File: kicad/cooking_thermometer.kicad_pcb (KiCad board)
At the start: 2 copper layers, 75.5 x 40.4 mm, 60 parts, among them J1 FTDI, J2 STLINK, J3 3V3_Power, J4 Battery, J6 OLED_CONN, J7 5V_Power, J8 THERMO_CONN, J9 USB_C, Q1 BC547, SW1 BOOT0_SW, SW2 NRST_SW, SW3 UI_A_SW, SW4 UI_B_SW, SW5 UI_C_SW, U1 STM32G0B0KETx, U2 MCP1700x-330xxTO, U3 MCP73831-2-OT

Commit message: Final silk fixes
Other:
- board text added: "5V"
- board text added: "A"
- board text added: "B"
- board text added: "BOOT0"
- board text added: "C"
- board text added: "RST"
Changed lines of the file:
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@@
 		(tags "tact sw push 6mm")
 		(property "Reference" "SW4"
-			(at 3.25 -2 0)
+			(at 6.388 -1.95 0)
 			(layer "F.SilkS")
 			(effects
@@
 		(tags "tact sw push 6mm")
 		(property "Reference" "SW5"
-			(at 3.25 -2 0)
+			(at 6.348 -2 0)
 			(layer "F.SilkS")
 			(effects
@@
 		(tags "mounting hole 3.2mm no annular m3")
 		(property "Reference" "H5"
-			(at 0 -4.2 0)
+			(at 4.6 1.1 0)
 			(layer "F.SilkS")
 			(effects
@@
 		(tags "Through hole pin header THT 1x02 2.54mm single row")
 		(property "Reference" "J7"
-			(at 0.25 -2.33 0)
+			(at 0.15 -2.46 0)
 			(layer "F.SilkS")
 			(effects
@@
 		(tags "tact sw push 6mm")
 		(property "Reference" "SW1"
-			(at 3.25 -2 0)
+			(at -0.024 -2 0)
 			(layer "F.SilkS")
 			(effects
@@
 		(tags "tact sw push 6mm")
 		(property "Reference" "SW2"
-			(at 3.25 -2 0)
+			(at -0.01 -1.994 0)
 			(layer "F.SilkS")
 			(effects
@@
 		(tags "tact sw push 6mm")
 		(property "Reference" "SW3"
-			(at 3.25 -2 0)
+			(at 6.428 -1.95 0)
 			(layer "F.SilkS")
 			(effects
@@
 		)
 	)
+	(gr_text "C"
+		(at 190.4 115.2 0)
+		(layer "F.SilkS")
+		(effects
+			(font
+				(size 1 1)
+				(thickness 0.15)
+			)
+		)
+	)
 	(gr_text "FTDI"
 		(at 149 86.5 90)
@@
 		)
 	)
+	(gr_text "BOOT0"
+		(at 200.5 77.6 0)
+		(layer "F.SilkS")
+		(effects
+			(font
+				(size 1 1)
+				(thickness 0.15)
+			)
+			(justify left bottom)
+		)
+	)
 	(gr_text "1"
 		(at 184.972 77.918 0)
@@
 		)
 	)
+	(gr_text "RST"
+		(at 189.9 77.6 0)
+		(layer "F.SilkS")
+		(effects
+			(font
+				(size 1 1)
+				(thickness 0.15)
+			)
+			(justify left bottom)
+		)
+	)
 	(gr_text "CHG"
 		(at 154.75 79.25 0)
@@
 		)
 	)
+	(gr_text "A"
+		(at 170.2 115.2 0)
+		(layer "F.SilkS")
+		(effects
+			(font
+				(size 1 1)
+				(thickness 0.15)
+			)
+		)
+	)
 	(gr_text "-"
 		(at 149.056 95.226 90)
@@
 		)
 	)
+	(gr_text "5V"
+		(at 160.6 107.4 0)
+		(layer "F.SilkS")
+		(effects
+			(font
+				(size 1 1)
+				(thickness 0.15)
+			)
+		)
+	)
 	(gr_text "PWR"
 		(at 159 79.25 0)
@@
 		)
 	)
+	(gr_text "B"
+		(at 180.2 115.2 0)
+		(layer "F.SilkS")
+		(effects
+			(font
+				(size 1 1)
+				(thickness 0.15)
+			)
+		)
+	)

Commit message: Create all necessary outputs for rev1 production
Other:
- board size 75.5 x 40.4 mm -> 75 x 40 mm
- board text added: "Rev1"
- board text added: "WayWayWay"
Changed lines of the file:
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@@
 			(svgprecision 4)
 			(plotframeref no)
-			(viasonmask no)
+			(viasonmask yes)
 			(mode 1)
 			(useauxorigin no)
@@
 			(outputformat 1)
 			(mirror no)
-			(drillshape 1)
+			(drillshape 0)
 			(scaleselection 1)
-			(outputdirectory "")
+			(outputdirectory "prod_outputs/rev1/")
 		)
 	)
@@
 		(tags "capacitor handsolder")
 		(property "Reference" "C3"
-			(at -3.302 0.254 180)
+			(at -3.182 1.8 180)
 			(layer "F.SilkS")
 			(effects
@@
 		(tags "capacitor handsolder")
 		(property "Reference" "C1"
-			(at 3.2135 0 180)
+			(at 0.0875 1.942 -90)
 			(layer "F.SilkS")
 			(effects
@@
 	)
 	(gr_rect
-		(start 147.146 75.946)
-		(end 222.598 116.332)
+		(start 147.4 76.2)
+		(end 222.4 116.2)
 		(stroke
 			(width 0.05)
@@
 		)
 	)
+	(gr_text "WayWayWay"
+		(at 216.8 114.3 0)
+		(layer "F.SilkS")
+		(effects
+			(font
+				(size 1 1)
+				(thickness 0.15)
+			)
+		)
+	)
 	(gr_text "STLink"
 		(at 176.5 77.5 0)
@@
 		)
 	)
+	(gr_text "Rev1"
+		(at 150.2 114.5 0)
+		(layer "F.SilkS")
+		(effects
+			(font
+				(size 1 1)
+				(thickness 0.15)
+			)
+		)
+	)
 	(gr_text "PWR"
 		(at 159 79.25 0)
@@
 		(polygon
 			(pts
-				(xy 147.654 76.204) (xy 222.09 76.454) (xy 222.09 115.824) (xy 147.654 115.574)
+				(xy 147.7 76.4) (xy 222.09 76.454) (xy 222.09 115.824) (xy 147.7 115.8)
 			)
 		)

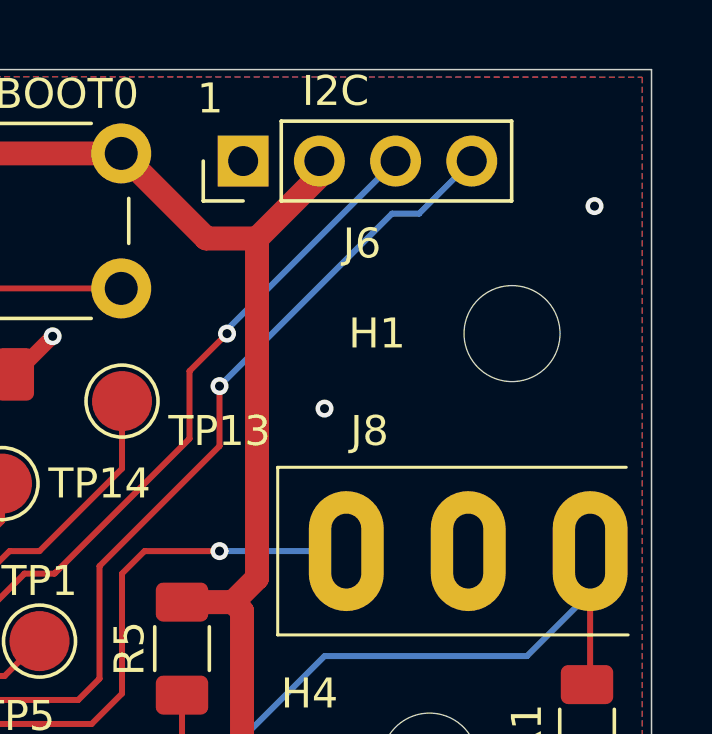
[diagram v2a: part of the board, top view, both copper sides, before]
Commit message: Update schematic and board
Add C5 for temperature input stabilization

Rename UI led and buzzer to correctly denote PWM usage
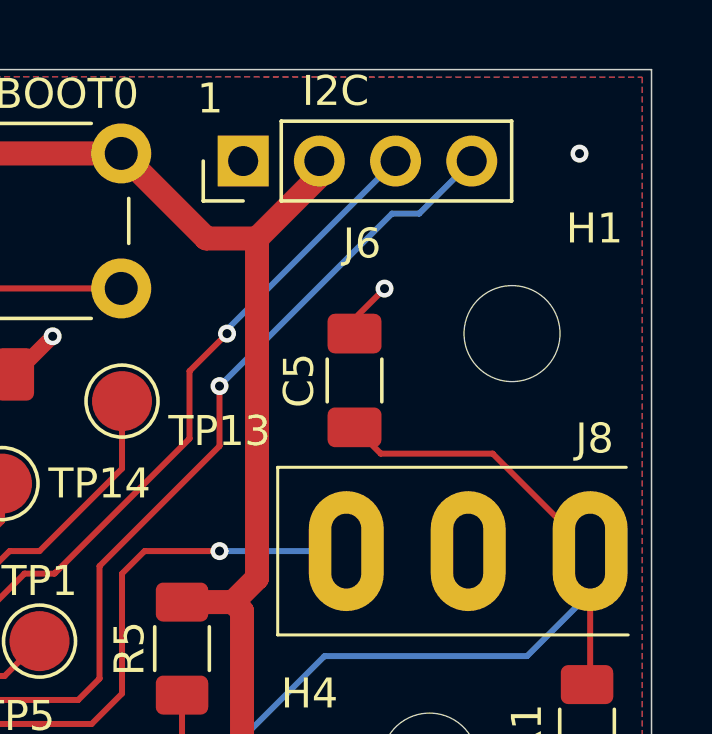
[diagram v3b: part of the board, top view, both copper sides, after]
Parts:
- added C5: 1uF, Capacitor_SMD:C_1206_3216Metric_Pad1.33x1.80mm_HandSolder, F.Cu at (212.5, 86.6)
- BZ1: value Passive_Buzzer -> Active_Buzzer
- R8, R9: value 100k -> 10k
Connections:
- net /TIM3_CH2_BUZZER_PWM renamed /BUZZER_ON
- net /UI_LED renamed /TIM3_CH1_UI_LED_PWM
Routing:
- net /ADC10_TEMP_MEAS: track 36.5 -> 46.1 mm
- net GND: track 65.3 -> 67.2 mm
